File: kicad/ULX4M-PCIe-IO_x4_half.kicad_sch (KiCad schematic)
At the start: 13 parts, among them J3 SFP+, J4 SFP+, J5 Conn_02x20_Odd_Even, J6 Conn_02x05_Odd_Even, J7 Micro_SD_Card_CD, J8 Conn_02x05_Odd_Even, P1 HDMI-D, P2 HDMI-D, SW1 SW_DIP_x08, SW2 SW_DIP_x08, U1 Raspberry_Pi_Compute_Module_4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

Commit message: Modules update
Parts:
- removed U1: Raspberry_Pi_Compute_Module_4_Compute_Module_4_Fu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, cm4:Raspberry-Pi-4-Compute-Module, symbol PCIexpress_x4_half-rescue:Raspberry_Pi_Compute_Module_4_Compute_Module_4_Functi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
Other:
- added sheet CM4_module (CM4_module.kicad_sch)
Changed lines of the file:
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@@
-    )
-  )
-  (symbol (lib_id "PCIexpress_x4_half-rescue:Raspberry_Pi_Compute_Module_4_Compute_Module_4_Functional-cm4-carrier-template-cache") (at 114.935 31.115 0) (unit 5)
-    (in_bom yes) (on_board yes) (dnp no)
-    (property "Reference" "U1" (at 132.9182 23.8252 0)
-      (effects (font (size 1.524 1.524)))
-    )
-    (property "Value" "Raspberry_Pi_Compute_Module_4_Compute_Module_4_Functional" (at 132.9182 26.5176 0)
-      (effects (font (size 1.524 1.524)))
-    )
-    (property "Footprint" "cm4:Raspberry-Pi-4-Compute-Module" (at 120.015 29.845 0)
-      (effects (font (size 1.524 1.524)) (justify left) hide)
-    )
-    (property "Datasheet" "" (at 120.015 34.925 0)
-      (effects (font (size 1.524 1.524)) (justify left) hide)
-    )
-    (instances
-      (project "ULX4M-PCIe-IO_x4_half"
-        (path "/e227bafe-08dc-4b2a-9df8-340d24e6faf1"
-          (reference "U1") (unit 5) (value "Raspberry_Pi_Compute_Module_4_Compute_Module_4_Functional") (footprint "cm4:Raspberry-Pi-4-Compute-Module")
-        )
-      )
     )
   )
@@
     (pin "PER0_P" input (at 34.29 58.42 180)
       (effects (font (size 1.27 1.27)) (justify left))
+    )
+  )
+  (sheet (at 92.71 48.26) (size 36.83 29.21) (fields_autoplaced)
+    (stroke (width 0.1524) (type solid) (color 132 0 132 1))
+    (fill (color 255 255 255 0.0000))
+    (property "Sheetname" "CM4_module" (at 92.71 47.5484 0)
+      (effects (font (size 1.27 1.27)) (justify left bottom))
+    )
+    (property "Sheetfile" "CM4_module.kicad_sch" (at 92.71 78.0546 0)
+      (effects (font (size 1.27 1.27)) (justify left top))
     )
   )
@@
     (path "/e227bafe-08dc-4b2a-9df8-340d24e6faf1/00000000-0000-0000-0000-00005d508b15/00000000-0000-0000-0000-00005dbb44a0" (page "9"))
     (path "/e227bafe-08dc-4b2a-9df8-340d24e6faf1/00000000-0000-0000-0000-00005d508b15/00000000-0000-0000-0000-00005d516dfb" (page "10"))
+    (path "/e227bafe-08dc-4b2a-9df8-340d24e6faf1/aaee048f-74e7-455f-95c1-2be2b9e5c5ad" (page "11"))
   )
 )

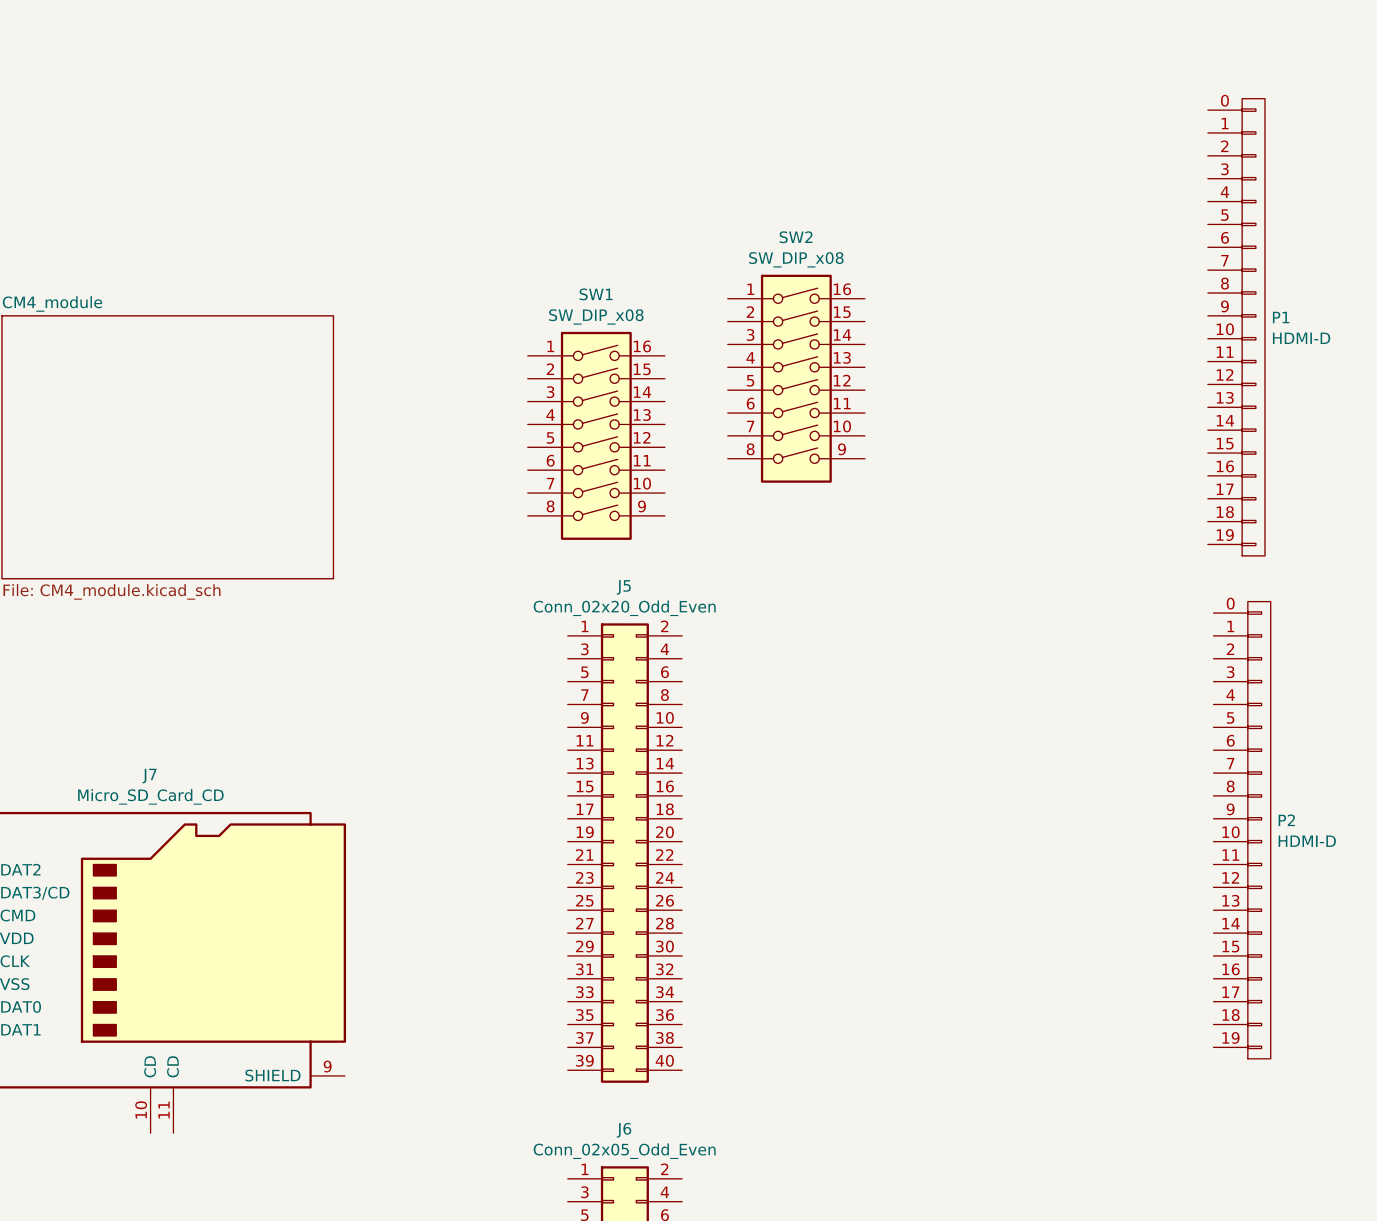
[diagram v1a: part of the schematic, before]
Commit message: Adding SPDIF
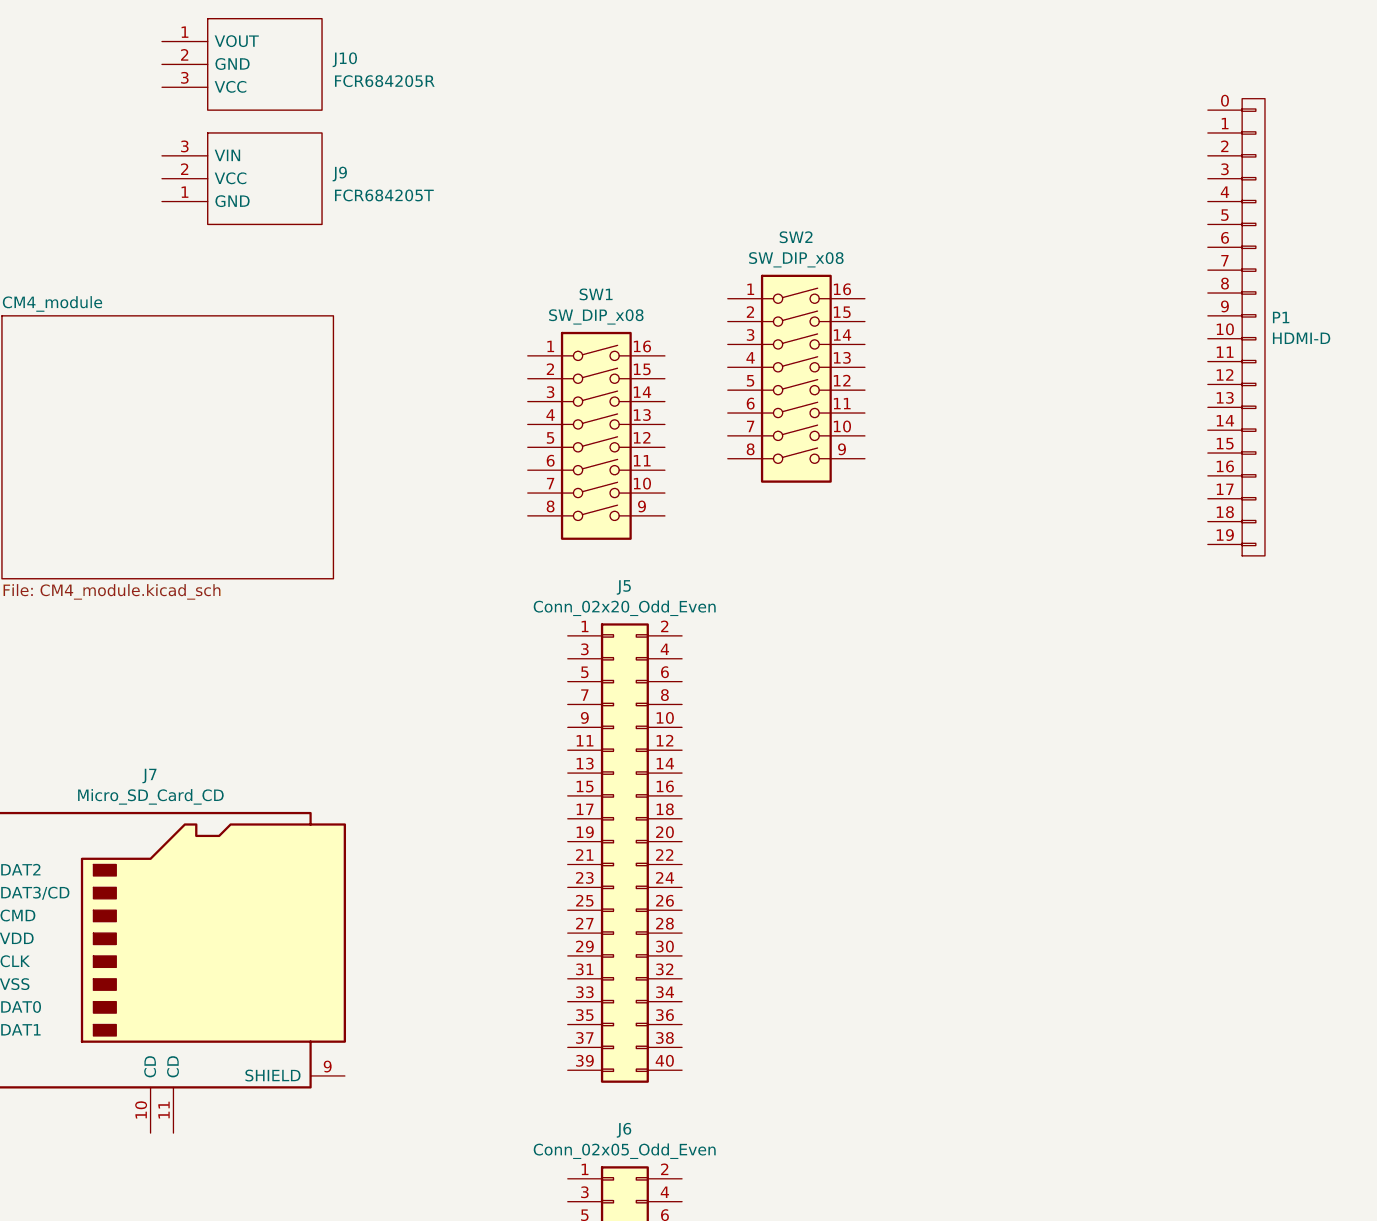
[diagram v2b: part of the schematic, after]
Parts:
- removed P2: HDMI-D, hdmi-d:HDMI-D, symbol hdmi-d:HDMI-D
- added J10: FCR684205R, FCR684205-R:FCR684205R, symbol FCR684205R:FCR684205R
- added J9: FCR684205T, FCR684205-T:FCR684205T, symbol FCR684205T:FCR684205T
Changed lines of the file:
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@@
-    )
-  )
-  (symbol (lib_id "hdmi-d:HDMI-D") (at 232.41 105.41 0) (unit 1)
-    (in_bom yes) (on_board yes) (dnp no)
-    (property "Reference" "P2" (at 234.3912 104.3686 0)
-      (effects (font (size 1.27 1.27)) (justify left))
-    )
-    (property "Value" "HDMI-D" (at 234.3912 106.68 0)
-      (effects (font (size 1.27 1.27)) (justify left))
-    )
-    (property "Footprint" "hdmi-d:HDMI-D" (at 232.41 105.41 0)
-      (effects (font (size 1.524 1.524)) hide)
-    )
-    (property "Datasheet" "" (at 232.41 105.41 0)
-      (effects (font (size 1.524 1.524)))
-    )
-    (pin "0")
-    (pin "1")
-    (pin "10")
-    (pin "11")
-    (pin "12")
-    (pin "13")
-    (pin "14")
-    (pin "15")
-    (pin "16")
-    (pin "17")
-    (pin "18")
-    (pin "19")
-    (pin "2")
-    (pin "3")
-    (pin "4")
-    (pin "5")
-    (pin "6")
-    (pin "7")
-    (pin "8")
-    (pin "9")
-    (instances
-      (project "ULX4M-PCIe-IO_x4_half"
-        (path "/e227bafe-08dc-4b2a-9df8-340d24e6faf1"
-          (reference "P2") (unit 1) (value "HDMI-D") (footprint "hdmi-d:HDMI-D")
-        )
-      )
     )
   )
@@
         )
       )
+    )
+  )
+  (symbol (lib_id "FCR684205T:FCR684205T") (at 110.49 30.48 0) (unit 1)
+    (in_bom yes) (on_board yes) (dnp no) (fields_autoplaced)
+    (property "Reference" "J9" (at 129.54 32.385 0)
+      (effects (font (size 1.27 1.27)) (justify left))
+    )
+    (property "Value" "FCR684205T" (at 129.54 34.925 0)
+      (effects (font (size 1.27 1.27)) (justify left))
+    )
+    (property "Footprint" "FCR684205-T:FCR684205T" (at 129.54 27.94 0)
+      (effects (font (size 1.27 1.27)) (justify left) hide)
+    )
+    (property "Datasheet" "https://www.cliffuk.co.uk/products/optical/FCR684205T.pdf" (at 129.54 30.48 0)
+      (effects (font (size 1.27 1.27)) (justify left) hide)
+    )
+    (property "Description" "Fiber Optic Transmitter with Driver 655nm 16Mbps 2.7V ~{} 5.5V 10 mA" (at 129.54 33.02 0)
+      (effects (font (size 1.27 1.27)) (justify left) hide)
+    )
+    (property "Height" "19.2" (at 129.54 35.56 0)
+      (effects (font (size 1.27 1.27)) (justify left) hide)
+    )
+    (property "Manufacturer_Name" "CLIFF ELECTRONIC COMPONENTS" (at 129.54 38.1 0)
+      (effects (font (size 1.27 1.27)) (justify left) hide)
+    )
+    (property "Manufacturer_Part_Number" "FCR684205T" (at 129.54 40.64 0)
+      (effects (font (size 1.27 1.27)) (justify left) hide)
+    )
+    (property "Mouser Part Number" "" (at 129.54 43.18 0)
+      (effects (font (size 1.27 1.27)) (justify left) hide)
+    )
+    (property "Mouser Price/Stock" "" (at 129.54 45.72 0)
+      (effects (font (size 1.27 1.27)) (justify left) hide)
+    )
+    (property "Arrow Part Number" "" (at 129.54 48.26 0)
+      (effects (font (size 1.27 1.27)) (justify left) hide)
+    )
+    (property "Arrow Price/Stock" "" (at 129.54 50.8 0)
+      (effects (font (size 1.27 1.27)) (justify left) hide)
+    )
+    (property "Mouser Testing Part Number" "" (at 129.54 53.34 0)
+      (effects (font (size 1.27 1.27)) (justify left) hide)
+    )
+    (property "Mouser Testing Price/Stock" "" (at 129.54 55.88 0)
+      (effects (font (size 1.27 1.27)) (justify left) hide)
+    )
+    (pin "1")
+    (pin "2")
+    (pin "3")
+    (instances
+      (project "ULX4M-PCIe-IO_x4_half"
+        (path "/e227bafe-08dc-4b2a-9df8-340d24e6faf1"
+          (reference "J9") (unit 1) (value "FCR684205T") (footprint "FCR684205-T:FCR684205T")
+        )
+      )
+    )
+  )
+  (symbol (lib_id "FCR684205R:FCR684205R") (at 110.49 17.78 0) (unit 1)
+    (in_bom yes) (on_board yes) (dnp no) (fields_autoplaced)
+    (property "Reference" "J10" (at 129.54 19.685 0)
+      (effects (font (size 1.27 1.27)) (justify left))
+    )
+    (property "Value" "FCR684205R" (at 129.54 22.225 0)
+      (effects (font (size 1.27 1.27)) (justify left))
+    )
+    (property "Footprint" "FCR684205-R:FCR684205R" (at 129.54 15.24 0)
+      (effects (font (size 1.27 1.27)) (justify left) hide)
+    )
+    (property "Datasheet" "http://www.cliffuk.co.uk/products/optical/FCR684205R.pdf" (at 129.54 17.78 0)
+      (effects (font (size 1.27 1.27)) (justify left) hide)
+    )
+    (property "Description" "FIBER OPTIC DATA LINK" (at 129.54 20.32 0)
+      (effects (font (size 1.27 1.27)) (justify left) hide)
+    )
+    (property "Height" "19.2" (at 129.54 22.86 0)
+      (effects (font (size 1.27 1.27)) (justify left) hide)
+    )
+    (property "Manufacturer_Name" "CLIFF ELECTRONIC COMPONENTS" (at 129.54 25.4 0)
+      (effects (font (size 1.27 1.27)) (justify left) hide)
+    )
+    (property "Manufacturer_Part_Number" "FCR684205R" (at 129.54 27.94 0)
+      (effects (font (size 1.27 1.27)) (justify left) hide)
+    )
+    (property "Mouser Part Number" "" (at 129.54 30.48 0)
+      (effects (font (size 1.27 1.27)) (justify left) hide)
+    )
+    (property "Mouser Price/Stock" "" (at 129.54 33.02 0)
+      (effects (font (size 1.27 1.27)) (justify left) hide)
+    )
+    (property "Arrow Part Number" "" (at 129.54 35.56 0)
+      (effects (font (size 1.27 1.27)) (justify left) hide)
+    )
+    (property "Arrow Price/Stock" "" (at 129.54 38.1 0)
+      (effects (font (size 1.27 1.27)) (justify left) hide)
+    )
+    (property "Mouser Testing Part Number" "" (at 129.54 40.64 0)
+      (effects (font (size 1.27 1.27)) (justify left) hide)
+    )
+    (property "Mouser Testing Price/Stock" "" (at 129.54 43.18 0)
+      (effects (font (size 1.27 1.27)) (justify left) hide)
+    )
+    (pin "1")
+    (pin "2")
+    (pin "3")
+    (instances
+      (project "ULX4M-PCIe-IO_x4_half"
+        (path "/e227bafe-08dc-4b2a-9df8-340d24e6faf1"
+          (reference "J10") (unit 1) (value "FCR684205R") (footprint "FCR684205-R:FCR684205R")
+        )
+      )
